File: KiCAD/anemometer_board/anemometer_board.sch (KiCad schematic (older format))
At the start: 12 parts, among them J1 SOLAR, J2 BATT, U1 TCRT5000, U2 TC4056A_BREAKOUT, U3 LM393, U4 REGULATOR

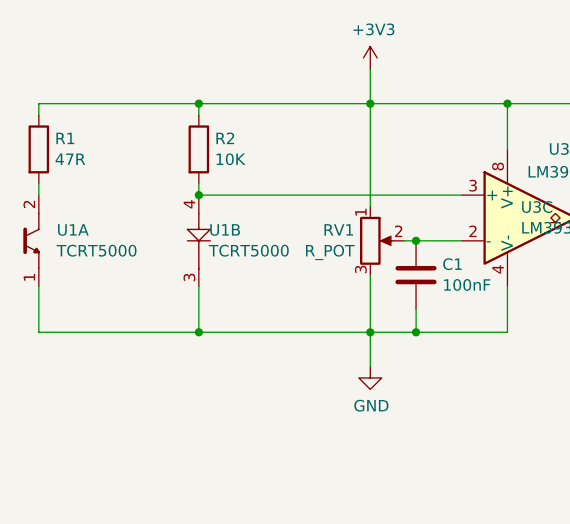
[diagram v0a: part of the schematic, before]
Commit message: Fix IR connections on PCB. Deploy as PCB V1.1
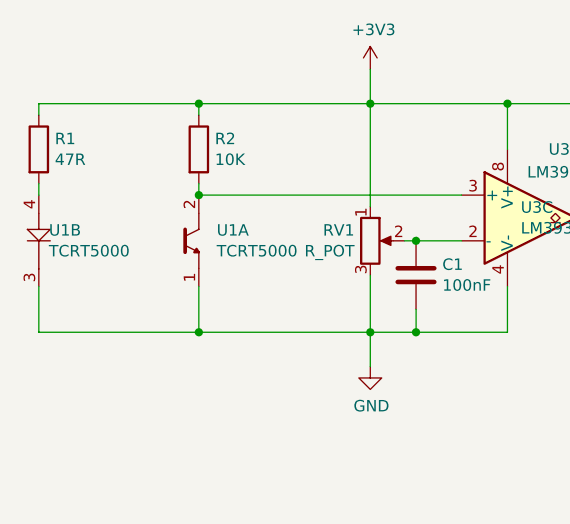
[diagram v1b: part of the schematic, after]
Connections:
- net at R2.2, U3.3 (+): now also U1.2; no longer U1.4
- net at R1.2: now also U1.4; no longer U1.2
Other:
- moved on the sheet: U1A, U1B
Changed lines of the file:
@@
 L sensors:TCRT5000 U1
 U 2 1 5F03B1B7
-P 1700 1600
-F 0 "U1" H 1744 1646 50  0000 L CNN
-F 1 "TCRT5000" H 1744 1555 50  0000 L CNN
-F 2 "headers:4x1" H 1470 1850 50  0001 C CNN
-F 3 "" H 1470 1850 50  0001 C CNN
-	2    1700 1600
+P 1000 1600
+F 0 "U1" H 1044 1646 50  0000 L CNN
+F 1 "TCRT5000" H 1044 1555 50  0000 L CNN
+F 2 "headers:4x1" H 770 1850 50  0001 C CNN
+F 3 "" H 770 1850 50  0001 C CNN
+	2    1000 1600
 	1    0    0    -1
 $EndComp
@@
 L sensors:TCRT5000 U1
 U 1 1 5F03C712
-P 1000 1600
-F 0 "U1" H 1078 1646 50  0000 L CNN
-F 1 "TCRT5000" H 1078 1555 50  0000 L CNN
-F 2 "headers:4x1" H 770 1850 50  0001 C CNN
-F 3 "" H 770 1850 50  0001 C CNN
-	1    1000 1600
+P 1700 1600
+F 0 "U1" H 1778 1646 50  0000 L CNN
+F 1 "TCRT5000" H 1778 1555 50  0000 L CNN
+F 2 "headers:4x1" H 1470 1850 50  0001 C CNN
+F 3 "" H 1470 1850 50  0001 C CNN
+	1    1700 1600
 	1    0    0    -1
 $EndComp
